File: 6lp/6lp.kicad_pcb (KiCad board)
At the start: 2 copper layers, 34 parts, among them J1 MODULE_HEADER, T1 2450BM15A0015, U1 AT86RF233, X1 16.0000MF09Z-AC3

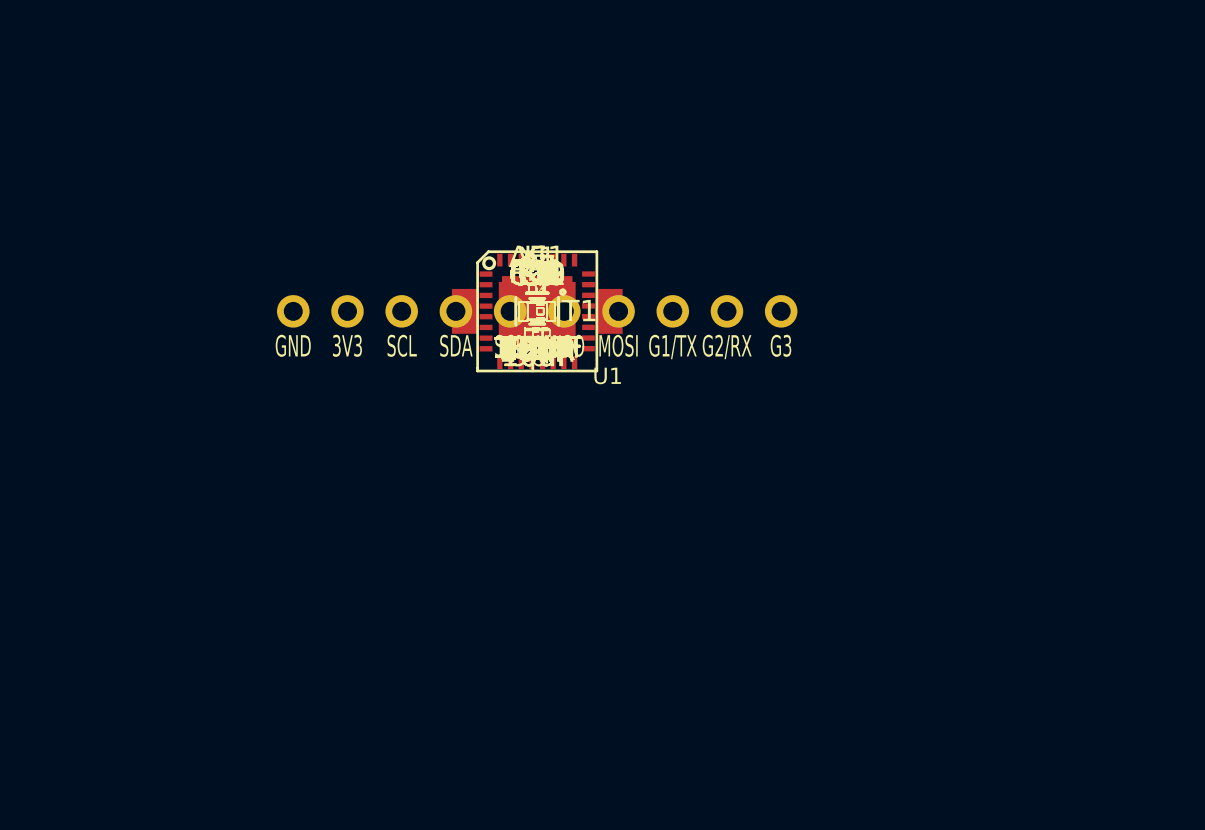
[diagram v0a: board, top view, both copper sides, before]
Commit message: board outline, header placement
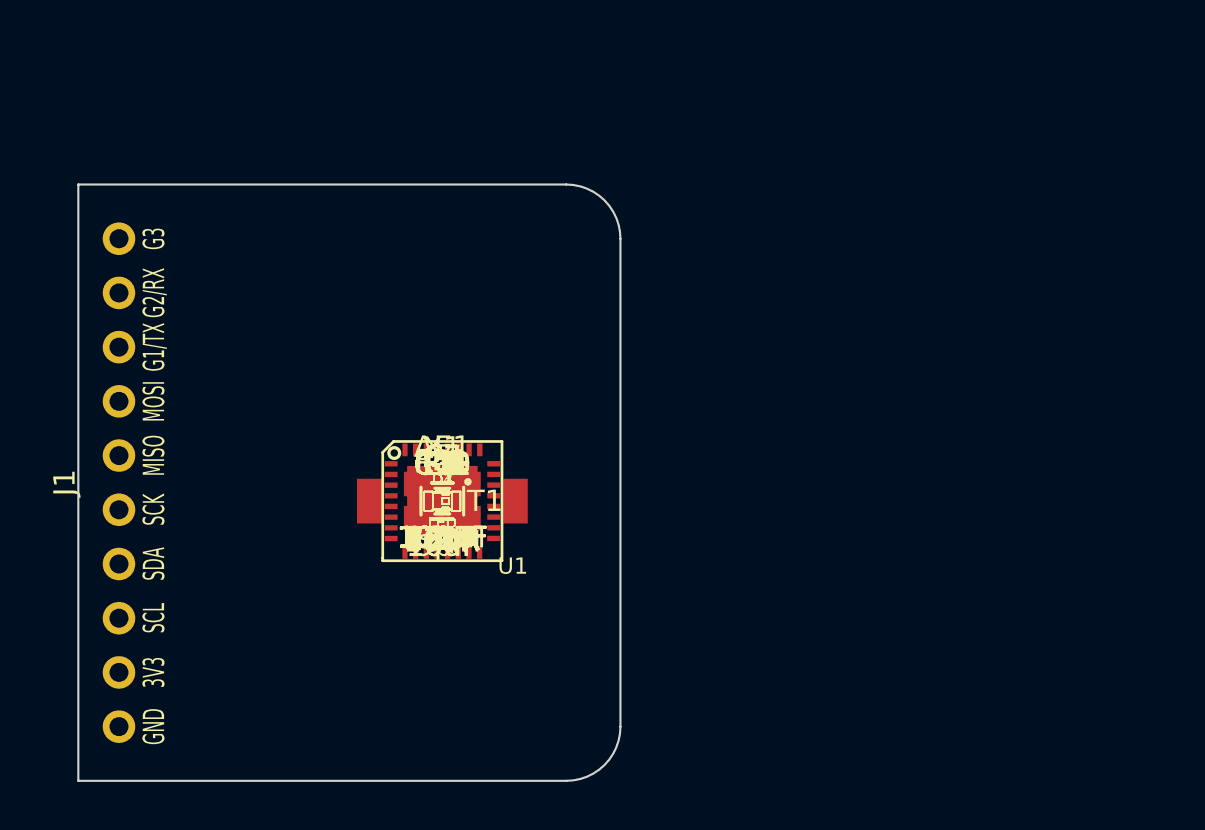
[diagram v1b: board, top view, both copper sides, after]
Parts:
- moved J1 21.2 mm to (128.9, 113.0), turned to 90 degrees
- moved AE1 9.94 mm to (144.1, 113.9)
- moved C1 9.94 mm to (144.1, 113.9)
- moved C10 9.94 mm to (144.1, 113.9)
- moved C11 9.94 mm to (144.1, 113.9)
- moved C12 9.94 mm to (144.1, 113.9)
- moved C13 9.94 mm to (144.1, 113.9)
- moved C2 9.94 mm to (144.1, 113.9)
- moved C3 9.94 mm to (144.1, 113.9)
- moved C4 9.94 mm to (144.1, 113.9)
- moved C5 9.94 mm to (144.1, 113.9)
- moved C6 9.94 mm to (144.1, 113.9)
- moved C7 9.94 mm to (144.1, 113.9)
- moved C8 9.94 mm to (144.1, 113.9)
- moved C9 9.94 mm to (144.1, 113.9)
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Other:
- board outline added: 25.4 x 27.9 mm

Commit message: invisible values
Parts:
- moved C8 32.8 mm to (176.5, 109.5)
- moved C11 27.0 mm to (170.7, 118.4)
- moved C7 26.8 mm to (168.4, 102.6)
- moved C12 26.1 mm to (169.7, 109.0)
- moved C2 22.0 mm to (160.3, 99.1)
- moved R7 21.6 mm to (133.1, 95.2)
- moved L1 20.4 mm to (162.8, 121.9)
- moved FB1 19.8 mm to (154.4, 97.0)
- moved R1 18.4 mm to (148.3, 96.0)
- moved C13 18.1 mm to (161.8, 110.2)
- moved R3 18.0 mm to (139.4, 96.5)
- moved C10 17.7 mm to (159.3, 104.9)
- moved R6 17.4 mm to (144.3, 96.5)
- moved T1 17.3 mm to (161.3, 114.8)
- moved X1 14.8 mm to (135.4, 101.9)
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
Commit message: placement round one...
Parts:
- C7: footprint Capacitors_SMD:C_0805 -> Capacitors_SMD:C_0402
- moved C8 38.0 mm to (139.1, 115.6)
- moved C7 36.5 mm to (134.0, 114.7)
- moved FB1 32.8 mm to (133.1, 121.9)
- moved C11 26.3 mm to (145.3, 111.6), turned to 340 degrees
- moved R2 24.9 mm to (133.9, 103.6), turned to 90 degrees
- moved C10 24.4 mm to (137.7, 116.2), turned to 270 degrees
- moved C2 23.1 mm to (138.4, 106.6)
- moved C12 22.9 mm to (146.9, 112.0), turned to 45 degrees
- moved C1 22.1 mm to (134.7, 102.6), turned to 90 degrees
- moved D2 21.5 mm to (143.0, 103.3)
- moved D3 21.1 mm to (143.0, 104.8)
- moved T1 18.5 mm to (143.0, 112.3)
- moved L1 17.6 mm to (147.3, 113.7), turned to 110 degrees
- moved R1 17.3 mm to (132.6, 103.1)
- moved C3 16.5 mm to (137.8, 108.8)
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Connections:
- net Net-(R6-Pad1) renamed /CLKM
- C1 pad 1: Net-(C1-Pad1) -> /SLP/~RST
- J1 pad 10: /SLP/~RST -> /SLP/~RST~_IO
- R1 pad 1: /SLP/~RST -> /SLP/~RST~_IO
- R1 pad 2: Net-(C1-Pad1) -> /SLP/~RST
- R2 pad 2: Net-(C1-Pad1) -> /SLP/~RST
- R3 pad 1: Net-(C1-Pad1) -> /SLP/~RST
- R4 pad 2: Net-(C1-Pad1) -> /SLP/~RST
- R5 pad 2: Net-(C1-Pad1) -> /SLP/~RST
- T1 pad 3: /RFP -> /RFN
- T1 pad 4: /RFN -> /RFP

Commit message: closed project for review
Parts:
- added R11: 0, Resistors_SMD:R_0402, F.Cu at (137.9, 126.0)
- added R12: 0, Resistors_SMD:R_0402, F.Cu at (150.1, 108.7)
- moved R10 22.7 mm to (132.6, 125.0), turned to 180 degrees
- moved R9 22.7 mm to (132.6, 123.4), turned to 180 degrees
- moved D3 20.3 mm to (135.1, 123.4), turned to 180 degrees
- moved D4 20.3 mm to (135.1, 125.0), turned to 180 degrees
- moved FB1 6.25 mm to (138.7, 119.1), turned to 90 degrees
- moved D1 3.81 mm to (144.3, 105.3), turned to 90 degrees
- moved R8 2.83 mm to (142.7, 102.8), turned to 90 degrees
- moved D2 2.09 mm to (142.7, 105.3), turned to 90 degrees
- moved R7 1.65 mm to (144.3, 102.8), turned to 90 degrees
- moved AE1 1.02 mm to (148.7, 120.8)
- moved C12 1.02 mm to (148.0, 112.0)
- moved L1 1.02 mm to (148.3, 113.7)
- moved C11 1.02 mm to (146.3, 111.6)
- moved C13 1.02 mm to (149.2, 115.3)
- moved T1 1.02 mm to (144.0, 112.3)
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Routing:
- net AGND: track 0.00 -> 173.4 mm, vias 0 -> 42
- net DGND: track 0.00 -> 158.6 mm, vias 0 -> 33
- net +3.3V: track 0.00 -> 44.6 mm, vias 0 -> 1
- net /INTERRUPT: track 0.00 -> 20.0 mm
- net /DIG4: track 0.00 -> 15.9 mm, vias 0 -> 2
- net /~CS: track 0.00 -> 14.5 mm
- net /MOSI: track 0.00 -> 13.3 mm, vias 0 -> 2
- net /DIG3: track 0.00 -> 12.0 mm, vias 0 -> 2
- net /SCLK: track 0.00 -> 11.0 mm, vias 0 -> 1
- net /~RESET: track 0.00 -> 10.6 mm, vias 0 -> 2
- net /SLP_TR: track 0.00 -> 8.52 mm
- net /MISO: track 0.00 -> 6.72 mm
- net /DIG1: track 0.00 -> 6.55 mm
- net /XTAL1: track 0.00 -> 5.54 mm
- net /DIG2: track 0.00 -> 5.47 mm
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- added copper zone on B.Cu, net AGND
- added copper zone on F.Cu, net AGND
- added copper zone on B.Cu, net DGND
- added copper zone on F.Cu, net DGND
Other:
- net class Default: clearance 0.254 -> 0.2032; via_dia 0.889 -> 0.762; via_drill 0.635 -> 0.508
- rule trace_clearance: 0.254 -> 0.2032
- rule via_min_size: 0.889 -> 0.762
- board text added: "6lp-at86"

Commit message: gerbers
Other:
- rule pad_to_mask_clearance: 0 -> 0.0762
